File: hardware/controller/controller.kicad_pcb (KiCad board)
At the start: 2 copper layers, 30 x 100.5 mm, 29 parts, among them J1 DC_12V_IN, J2 HDD_POWER_OUT, J3 470531000, J4 470531000, J6 FH19C-7S-0.5SH10, Q1 2N3904, Q2 2N3904, U1 TSR0.5-2450, U2 XIAO-RP2350-SMD, U3 INA228, U4 74HC4051

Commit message: place all components on board
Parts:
- J1: moved to B.Cu
- moved J1 79.3 mm to (57.0, 116.5), turned to 180 degrees
- moved J2 65.9 mm to (56.3, 101.5), turned to -90 degrees
- moved U1 47.9 mm to (75.0, 86.1), turned to 180 degrees
- moved D1 28.3 mm to (73.5, 75.0)
- moved Q2 11.5 mm to (76.0, 132.1)
- moved J3 11.5 mm to (76.0, 97.5)
- moved J4 11.5 mm to (76.0, 118.0)
- moved Q1 11.5 mm to (76.0, 111.5)
- moved R10 11.5 mm to (70.0, 123.9)
- moved R5 11.5 mm to (70.5, 107.9)
- moved R6 11.5 mm to (70.5, 111.4)
- moved R7 11.5 mm to (70.5, 103.5)
- moved R8 11.5 mm to (70.0, 128.5)
- moved R9 11.5 mm to (70.0, 132.0)
- moved C3 2.83 mm to (62.0, 127.0)
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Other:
- board size 30 x 100.5 mm -> 30 x 100 mm

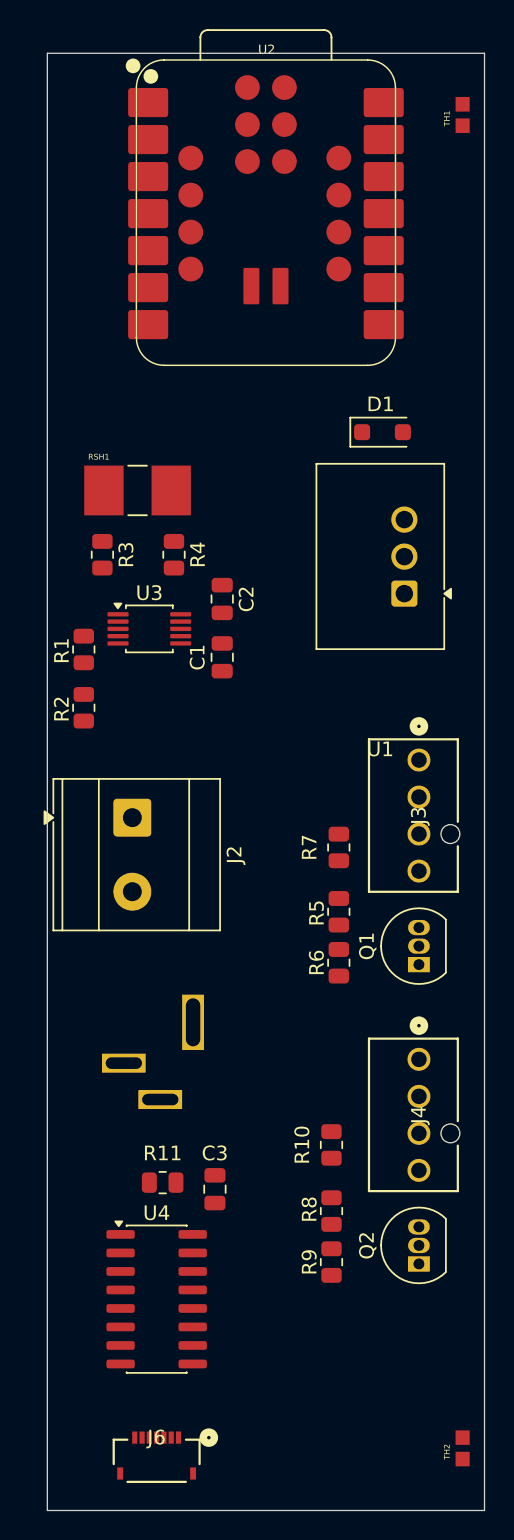
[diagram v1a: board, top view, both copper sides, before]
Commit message: initial attempt at tracing for controller, still need vias
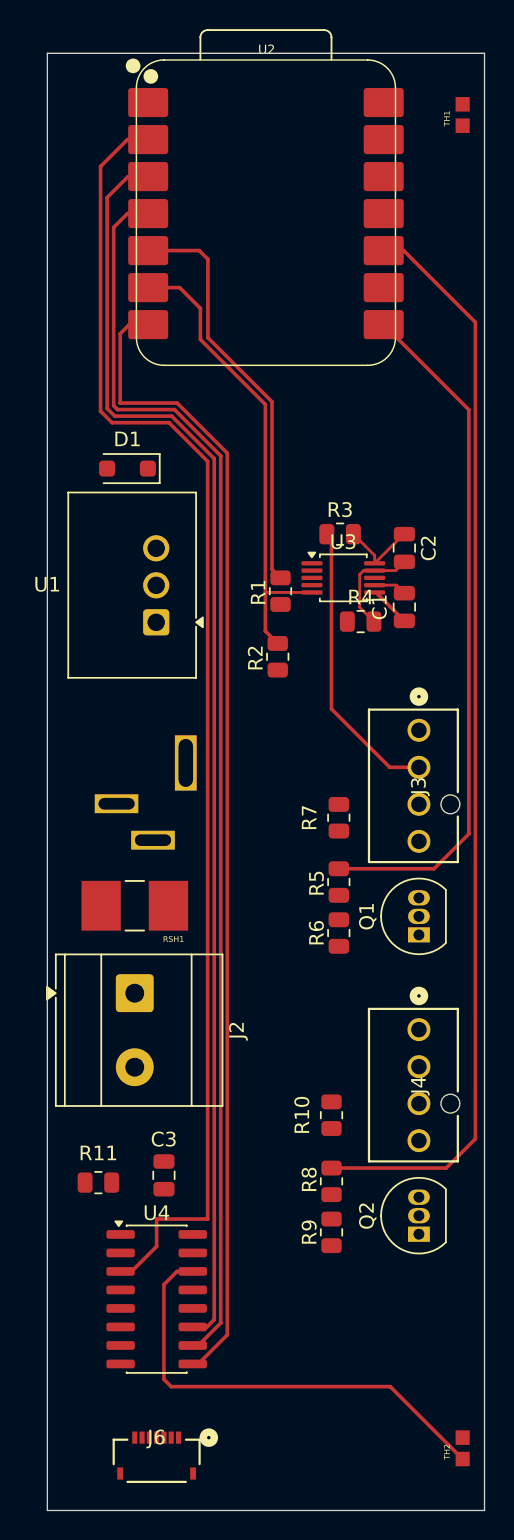
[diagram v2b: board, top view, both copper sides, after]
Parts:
- moved RSH1 28.5 mm to (56.5, 107.5), turned to 180 degrees
- moved J1 17.8 mm to (56.5, 98.7)
- moved D1 17.7 mm to (56.0, 77.5), turned to 180 degrees
- moved U1 17.1 mm to (58.0, 88.0)
- moved R3 16.4 mm to (70.6, 82.0), turned to 0 degrees
- moved R1 14.1 mm to (66.5, 85.9)
- moved R2 13.8 mm to (66.3, 90.4)
- moved U3 13.8 mm to (70.8, 85.0)
- moved R4 13.6 mm to (72.0, 88.0), turned to 0 degrees
- moved C2 13.0 mm to (75.0, 83.0)
- moved C1 13.0 mm to (75.0, 87.0)
- moved J2 12.0 mm to (56.5, 113.5)
- moved R11 4.41 mm to (54.0, 126.5)
- moved C3 3.63 mm to (58.5, 126.0)
- moved Q2 2.04 mm to (76.0, 130.0)
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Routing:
- net /NTC_ADC: track 0.00 -> 90.2 mm
- net /NTC_SEL0: track 0.00 -> 87.4 mm
- net /NTC_SEL1: track 0.00 -> 85.8 mm
- net /NTC_SEL2: track 0.00 -> 79.4 mm
- net /FAN2_PWM: track 0.00 -> 75.1 mm
- net /FAN1_PWM: track 0.00 -> 47.3 mm
- net /I2C_SCL: track 0.00 -> 32.6 mm
- net Net-(U4-A1): track 0.00 -> 31.6 mm
- net /I2C_SDA: track 0.00 -> 28.5 mm
- net /12V_IN: track 0.00 -> 19.8 mm
- net Net-(U3-Vin-): track 0.00 -> 7.06 mm
- net Net-(U3-Vin+): track 0.00 -> 5.47 mm
- net +3.3V: track 0.00 -> 2.85 mm
- net GND: track 0.00 -> 2.27 mm

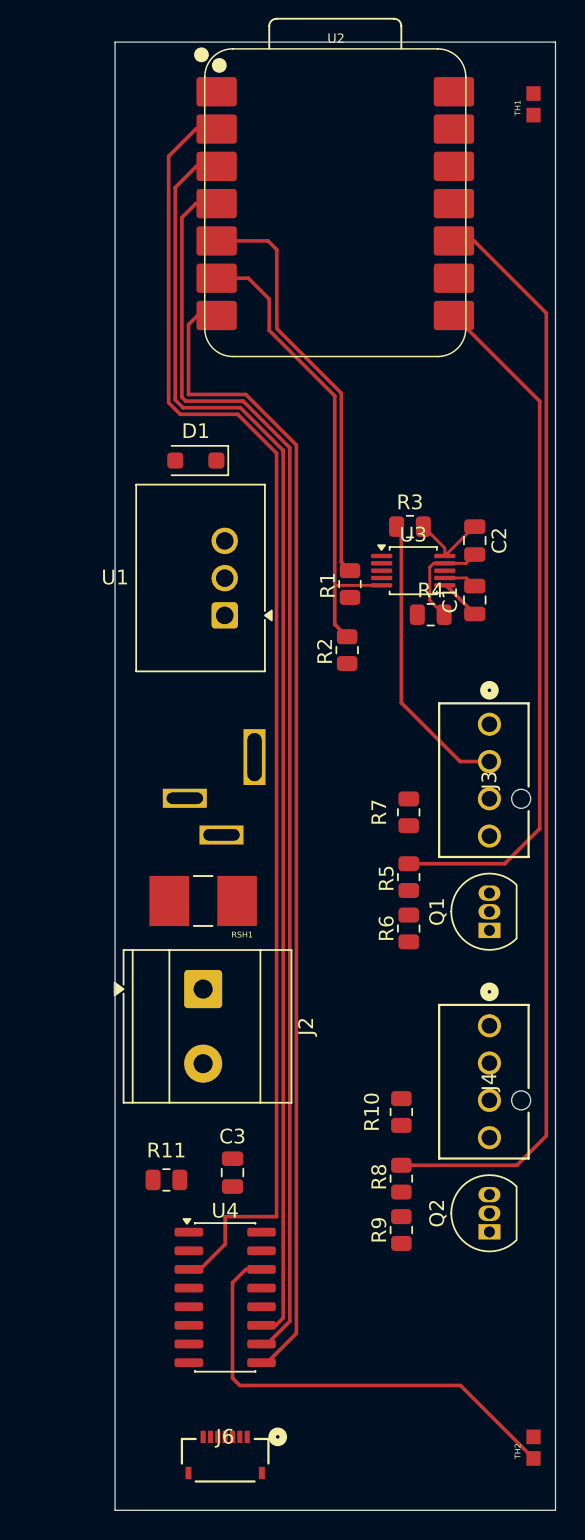
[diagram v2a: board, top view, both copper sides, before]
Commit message: finish routes for INA228
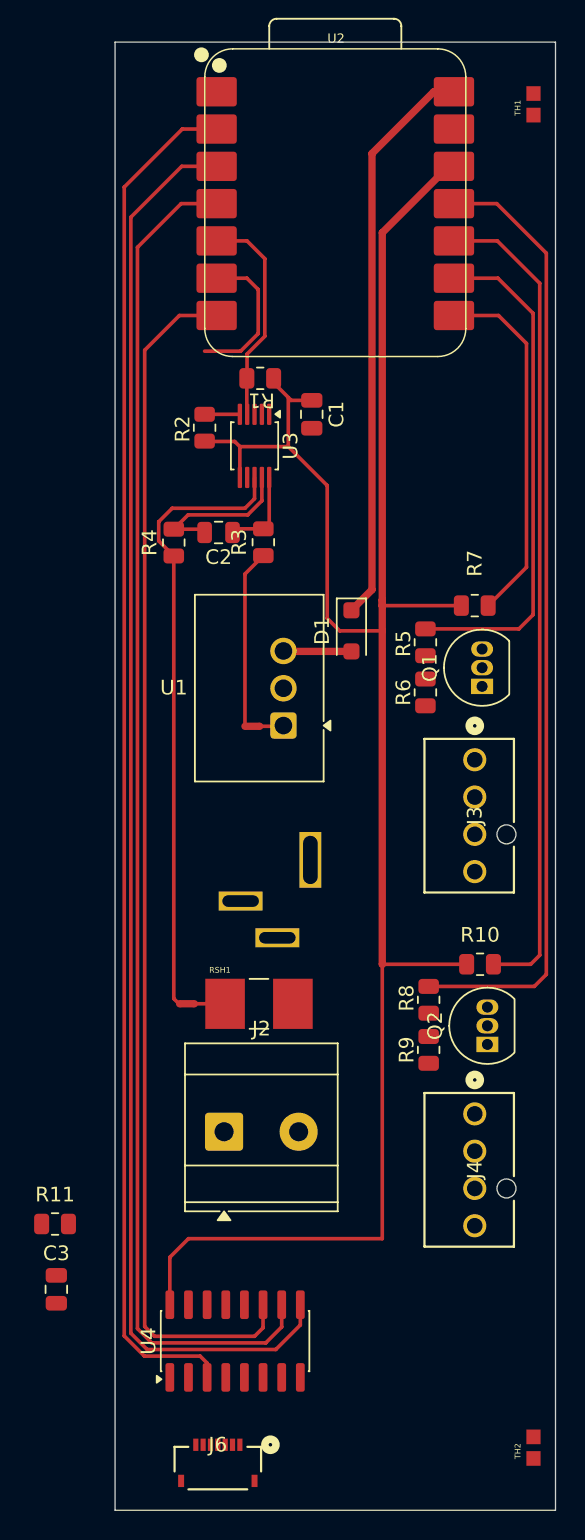
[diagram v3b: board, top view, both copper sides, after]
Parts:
- added NT1: NetTie_2, NetTie:NetTie-2_SMD_Pad0.5mm, F.Cu at (59.9, 95.6)
- added NT2: NetTie_2, NetTie:NetTie-2_SMD_Pad0.5mm, F.Cu at (55.4, 114.5)
- moved R4 18.2 mm to (54.5, 83.1), turned to 90 degrees
- moved R2 18.0 mm to (56.6, 75.3)
- moved C2 17.5 mm to (57.5, 82.4), turned to 180 degrees
- moved C1 16.8 mm to (63.9, 74.3), turned to -90 degrees
- moved Q1 16.6 mm to (75.5, 92.9)
- moved R6 16.1 mm to (71.6, 93.3)
- moved R5 16.0 mm to (71.6, 89.9)
- moved D1 15.7 mm to (66.6, 89.1), turned to -90 degrees
- moved R1 15.3 mm to (60.4, 71.9), turned to 0 degrees
- moved R7 14.8 mm to (75.0, 87.4), turned to 180 degrees
- moved C3 14.4 mm to (46.5, 133.9)
- moved U3 13.8 mm to (60.0, 76.5), turned to -90 degrees
- moved Q2 12.8 mm to (75.9, 117.3)
- moved R9 12.4 mm to (71.9, 117.6)
- moved R8 12.3 mm to (71.9, 114.2)
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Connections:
- R3 pad 1: /12V_IN -> /12V_IN_SENSE
- R4 pad 1: /12V_HDD -> /12V_HDD_SENSE
- RSH1 pad 1: /12V_IN -> /12V_HDD
- RSH1 pad 2: /12V_HDD -> /12V_IN
- U2 pad 10: /FAN2_PWM -> /FAN2_TACH
- U2 pad 11: /FAN2_TACH -> /FAN2_PWM
- U2 pad 3: /NTC_SEL0 -> /NTC_SEL2
- U2 pad 7: /NTC_SEL2 -> /NTC_SEL0
- U2 pad 8: /FAN1_PWM -> /FAN1_TACH
- U2 pad 9: /FAN1_TACH -> /FAN1_PWM
- U3 pad 8: /12V_HDD -> /12V_HDD_SENSE
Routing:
- net +3.3V: track 2.85 -> 136.8 mm
- net /FAN2_TACH: track 0.00 -> 56.2 mm
- net /12V_HDD_SENSE: track 0.00 -> 42.0 mm
- net +5V: track 0.00 -> 39.0 mm
- net Net-(U4-A1): track 31.6 -> 0.00 mm
- net /FAN1_TACH: track 0.00 -> 24.7 mm
- net /I2C_SCL: track 32.6 -> 12.7 mm
- net /12V_IN: track 19.8 -> 1.49 mm
- net /NTC_SEL2: track 79.4 -> 97.4 mm
- net /I2C_SDA: track 28.5 -> 14.5 mm
- net /FAN1_PWM: track 47.3 -> 34.6 mm
- net /12V_IN_SENSE: track 0.00 -> 12.1 mm
- net /FAN2_PWM: track 75.1 -> 65.2 mm
- net /NTC_SEL1: track 85.8 -> 92.5 mm
- net /NTC_SEL0: track 87.4 -> 82.5 mm
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
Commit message: fix route for INA228 I2C
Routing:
- net /I2C_SCL: track 12.7 -> 15.6 mm
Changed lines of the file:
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@@
+	)
+	(segment
+		(start 56.6 72.5)
+		(end 60.25 68.85)
+		(width 0.25)
+		(layer "F.Cu")
+		(net "/I2C_SCL")
+	)
+	(segment
+		(start 56.6 74.35)
+		(end 56.6 72.5)
+		(width 0.25)
+		(layer "F.Cu")
+		(net "/I2C_SCL")
+	)
+	(segment
+		(start 59 74.35)
+		(end 59.0125 74.3375)
+		(width 0.25)
+		(layer "F.Cu")
+		(net "/I2C_SCL")
+	)
+	(segment
+		(start 56.6 74.35)
+		(end 59 74.35)
+		(width 0.25)
+		(layer "F.Cu")
+		(net "/I2C_SCL")
 	)
 	(segment
@@
 		(width 0.25)
 		(layer "F.Cu")
-		(net "/I2C_SCL")
-	)
-	(segment
-		(start 59 74.35)
-		(end 59.0125 74.3375)
-		(width 0.25)
-		(layer "F.Cu")
-		(net "/I2C_SCL")
-	)
-	(segment
-		(start 56.6 70.05)
-		(end 59.05 70.05)
-		(width 0.25)
-		(layer "F.Cu")
-		(net "/I2C_SCL")
-	)
-	(segment
-		(start 59.05 70.05)
-		(end 60.25 68.85)
-		(width 0.25)
-		(layer "F.Cu")
-		(net "/I2C_SCL")
-	)
-	(segment
-		(start 56.6 74.35)
-		(end 59 74.35)
-		(width 0.25)
-		(layer "F.Cu")

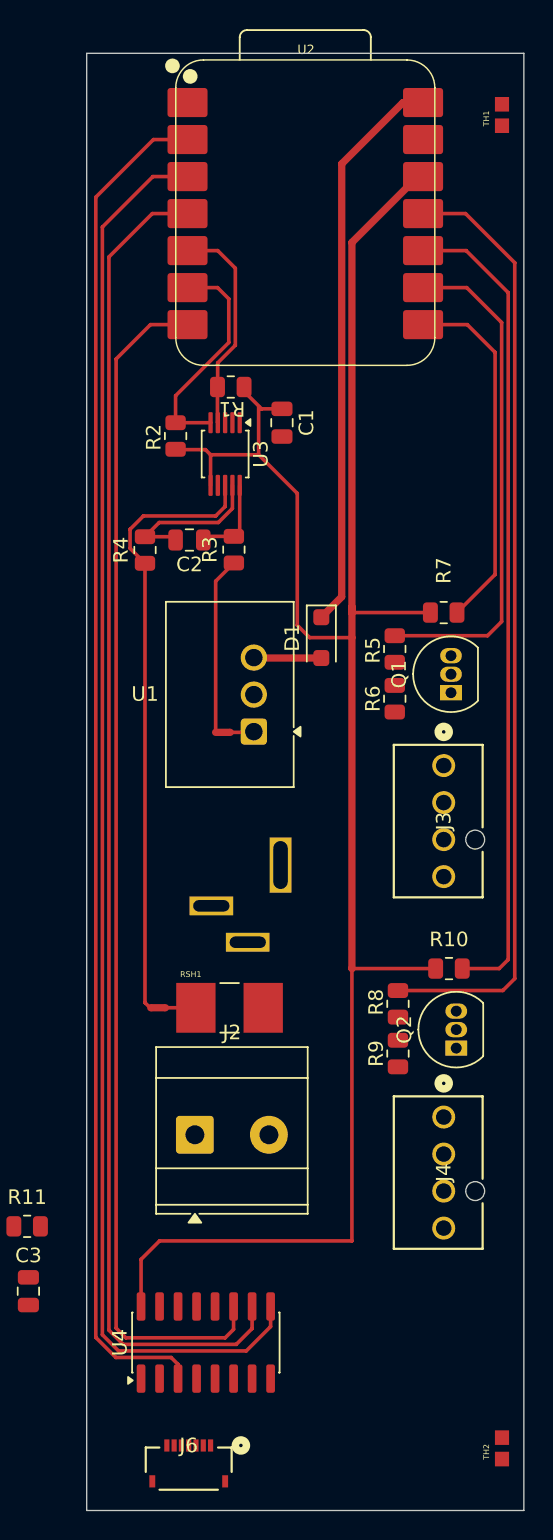
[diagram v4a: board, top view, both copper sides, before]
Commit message: add mounting holes
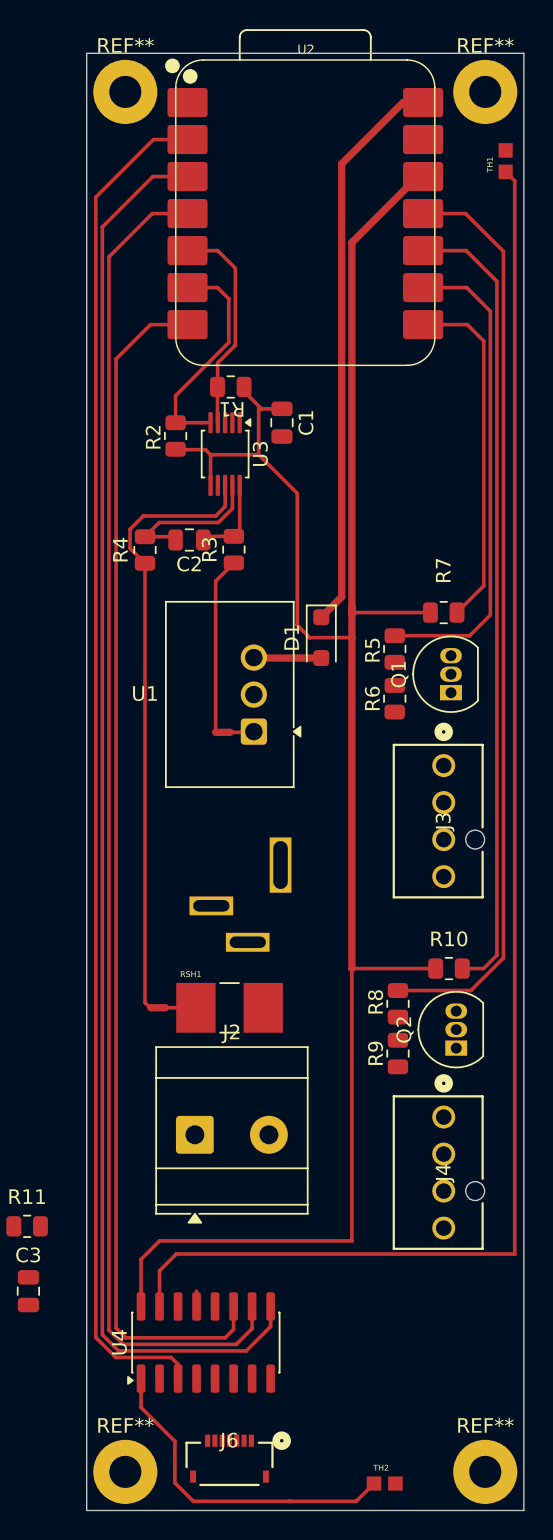
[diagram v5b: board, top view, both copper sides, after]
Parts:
- added REF**: MountingHole_2.2mm_M2_Pad, MountingHole:MountingHole_2.2mm_M2_Pad, F.Cu at (53.1, 51.6)
- added REF**: MountingHole_2.2mm_M2_Pad, MountingHole:MountingHole_2.2mm_M2_Pad, F.Cu at (77.8, 146.3)
- added REF**: MountingHole_2.2mm_M2_Pad, MountingHole:MountingHole_2.2mm_M2_Pad, F.Cu at (77.8, 51.6)
- added REF**: MountingHole_2.2mm_M2_Pad, MountingHole:MountingHole_2.2mm_M2_Pad, F.Cu at (53.1, 146.3)
- moved TH2 8.40 mm to (71.0, 147.2), turned to 0 degrees
- moved TH1 3.17 mm to (79.2, 56.4)
- moved J6 2.82 mm to (60.3, 145.8)
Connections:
- J6 pad 1: Net-(U4-A2) -> Net-(U4-A0)
- J6 pad 2: Net-(U4-A3) -> Net-(U4-A1)
- J6 pad 3: Net-(U4-A4) -> Net-(U4-A3)
- TH1 pad 1: Net-(U4-A0) -> /TH1
- TH2 pad 1: Net-(U4-A1) -> /TH2
- U4 pad 1: Net-(U4-A4) -> /TH2
- U4 pad 15: Net-(U4-A2) -> /TH1
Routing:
- net /TH1: track 0.00 -> 101.8 mm
- net /TH2: track 0.00 -> 22.9 mm
- net /FAN2_PWM: track 65.2 -> 63.2 mm
- net /FAN1_PWM: track 34.6 -> 33.3 mm
- net /FAN2_TACH: track 56.2 -> 54.9 mm
- net Net-(U4-A0): track 0.00 -> 1.04 mm
- net /FAN1_TACH: track 24.7 -> 24.0 mm

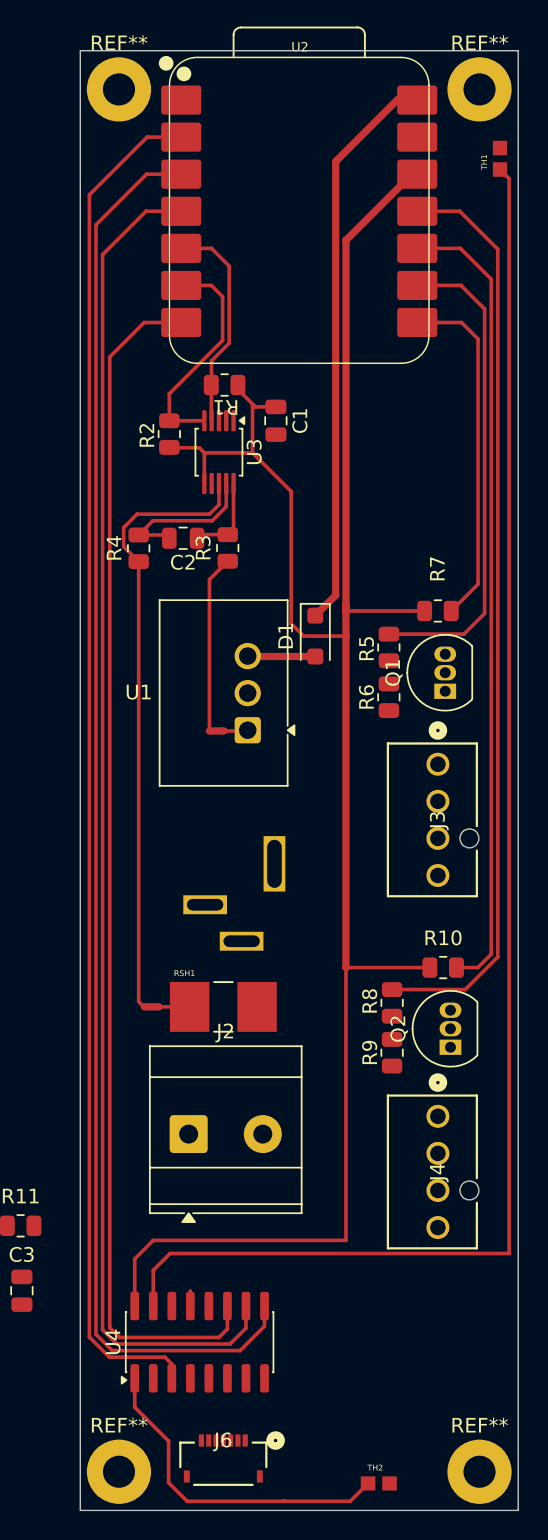
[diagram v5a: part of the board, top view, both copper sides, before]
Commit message: footprint template for JST
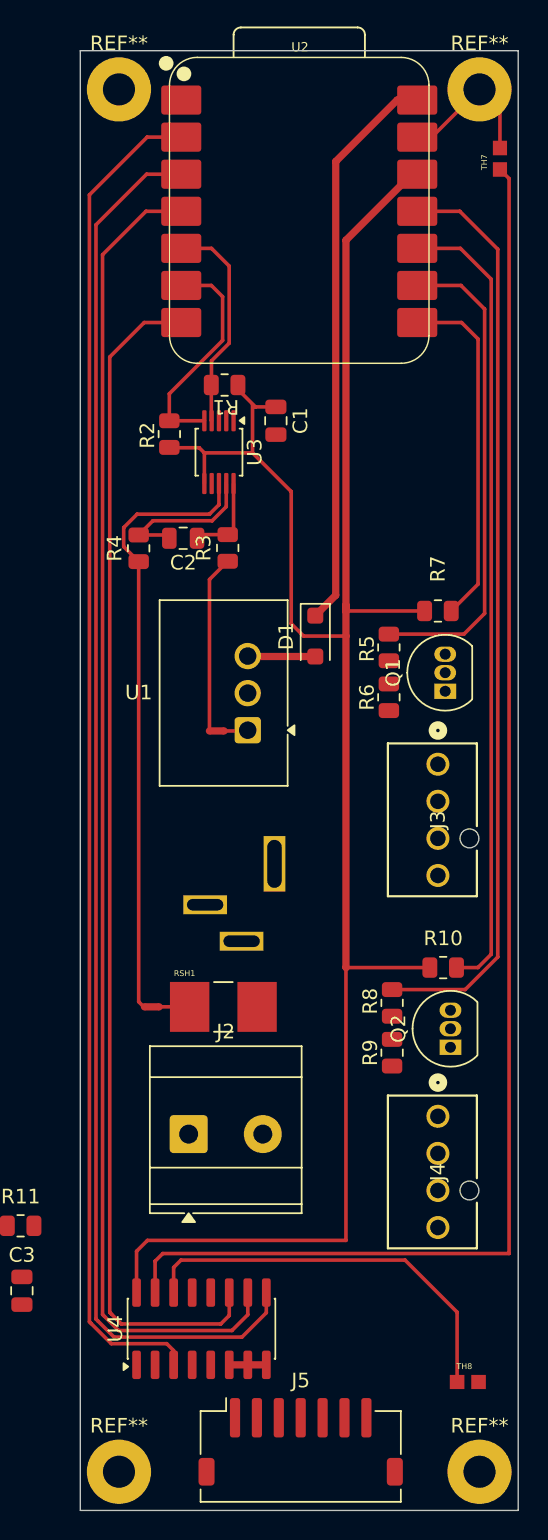
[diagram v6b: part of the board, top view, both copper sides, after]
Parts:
- removed J6: FH19C-7S-0.5SH10, Hirose_FH19C_7S_0_5SH:CONN7_FH19C_7S_HIR
- added J5: Conn_01x07, Connector_JST:JST_ZH_S7B-ZR-SM4A-TF_1x07-1MP_P1.50mm_Horizontal, F.Cu at (65.6, 144.3)
- moved TH8 9.25 mm to (77.0, 140.2)
- moved U4 0.93 mm to (58.8, 136.6)
- renumbered TH1 to TH7, TH2 to TH8
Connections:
- REF** pad 1: (no net) -> GND (x4)
- TH7 pad 1: /TH1 -> /TH7
- TH8 pad 1: /TH2 -> /TH8
- U4 pad 1: /TH2 -> /TH1
- U4 pad 12: Net-(U4-A3) -> /TH5
- U4 pad 13: Net-(U4-A0) -> /TH6
- U4 pad 14: Net-(U4-A1) -> /TH8
- U4 pad 15: /TH1 -> /TH7
- U4 pad 2: Net-(U4-A6) -> /TH2
- U4 pad 4: Net-(U4-A7) -> /TH3
- U4 pad 5: Net-(U4-A5) -> /TH4
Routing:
- net /TH1: track 101.8 -> 0.00 mm
- net /TH7: track 0.00 -> 101.1 mm
- net /TH8: track 0.00 -> 27.6 mm
- net /TH2: track 22.9 -> 0.00 mm
- net GND: track 0.00 -> 13.9 mm
- net Net-(U4-A0): track 1.04 -> 0.00 mm
- net /NTC_SEL2: track 97.4 -> 96.5 mm
- net /NTC_ADC: track 93.6 -> 92.7 mm
- net /NTC_SEL1: track 92.5 -> 91.6 mm
- net /NTC_SEL0: track 82.5 -> 81.7 mm
- net +3.3V: track 136.8 -> 136.0 mm

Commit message: update footprint for connector for thermistor strip
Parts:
- J5: footprint Connector_JST:JST_ZH_S7B-ZR-SM4A-TF_1x07-1MP_P1.50mm_Horizontal -> JST_ZH_S7B-ZR:JST_ZH_B7B-ZR_1x07_P1.50mm_Horizontal
- moved J5 5.33 mm to (70.9, 143.8), turned to 180 degrees
